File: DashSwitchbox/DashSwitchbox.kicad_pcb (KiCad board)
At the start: 2 copper layers, 16 parts, among them J1 Main Connector, J2 Estop Connector, J3 Dash LVMS, J4 To Drive Mode Button, J5 To Drive Mode Switch, J6 AMS Fault LED, J7 BSPD Fault LED, J8 IMD Fault LED, J9 Inertia Fault LED, U1 LD1117V33

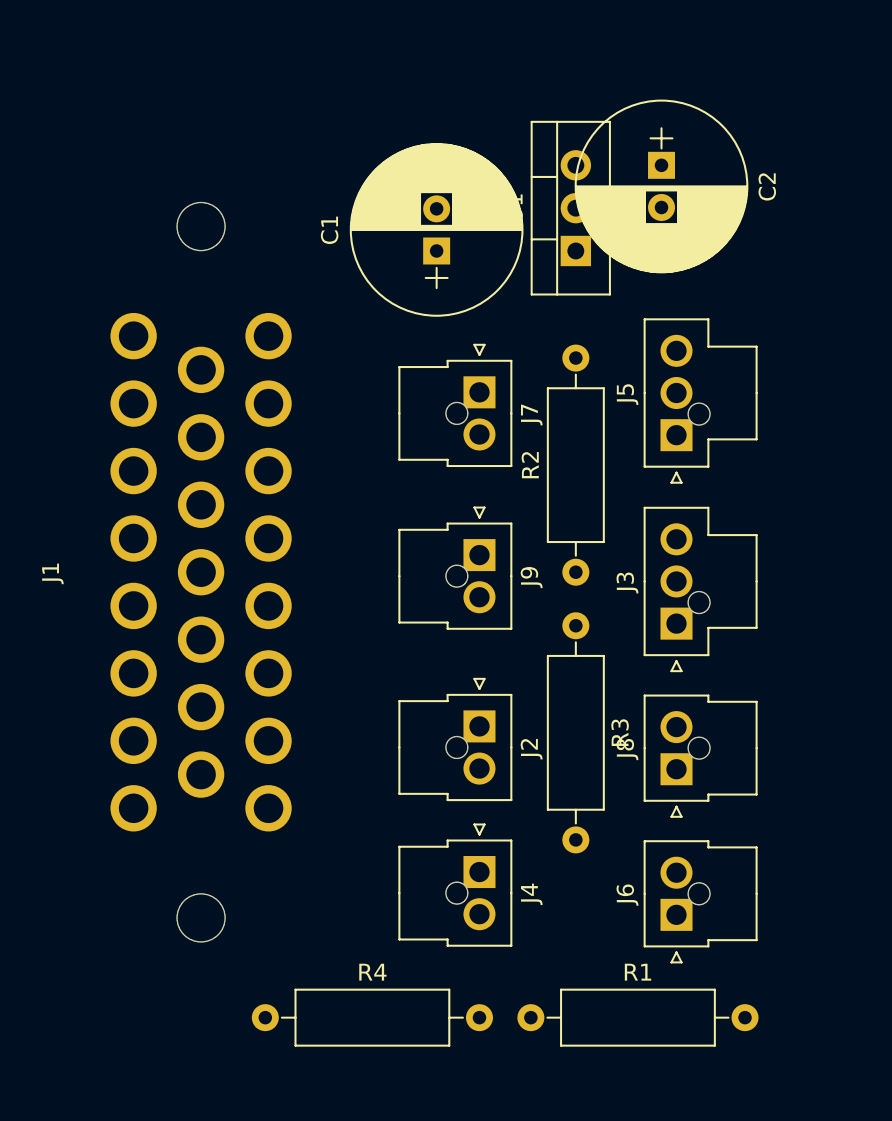
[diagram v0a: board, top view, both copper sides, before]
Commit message: Work for preparation for autorouting
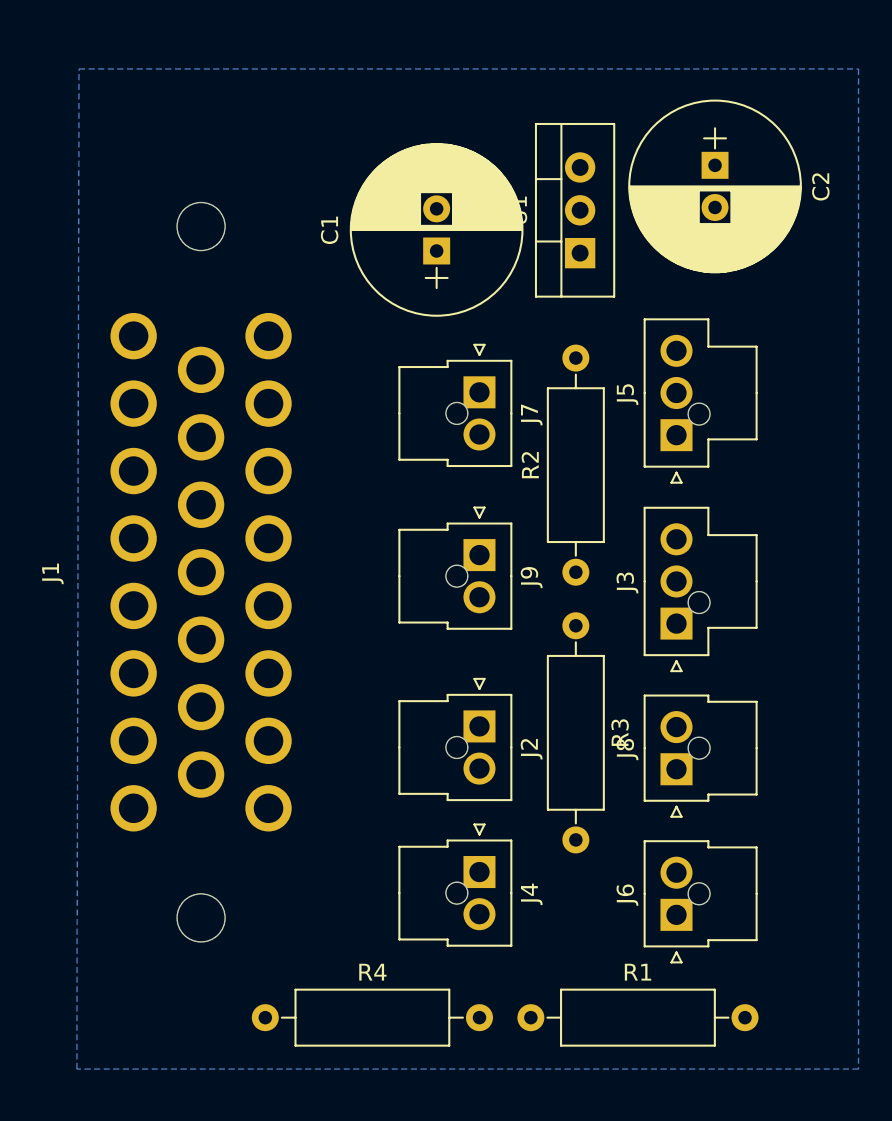
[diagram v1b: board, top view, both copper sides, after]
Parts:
- moved C2 3.17 mm to (123.2, 74.9)
- moved U1 0.28 mm to (115.2, 80.1)
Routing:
- added copper zone on B.Cu, net GND
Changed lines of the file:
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@@
     (links 36)
     (no_connects 36)
-    (area 0 0 0 0)
+    (area 82.845 68.384999 131.699001 129.735001)
     (thickness 1.6)
     (drawings 0)
@@
     (pad_to_mask_clearance 0)
     (aux_axis_origin 0 0)
-    (visible_elements FFFFFF7F)
+    (visible_elements 7FFFFFFF)
     (pcbplotparams
       (layerselection 0x00030_80000001)
@@
   )
   (module TO_SOT_Packages_THT:TO-220-3_Vertical (layer F.Cu)
-    (at 114.935 80.01 90)
+    (at 115.189 80.137 90)
     (descr "TO-220-3, Vertical, RM 2.54mm")
     (tags "TO-220-3 Vertical RM 2.54mm")
@@
   )
   (module Capacitors_THT:CP_Radial_D10.0mm_P2.50mm (layer F.Cu)
-    (at 120.015 74.93 270)
+    (at 123.19 74.93 270)
     (descr "CP, Radial series, Radial, pin pitch=2.50mm, , diameter=10mm, Electrolytic Capacitor")
     (tags "CP Radial series Radial pin pitch 2.50mm  diameter 10mm Electrolytic Capacitor")
@@
     )
   )
+  (zone (net 2) (net_name GND) (layer B.Cu) (hatch edge 0.508)
+    (connect_pads (clearance 0.508))
+    (min_thickness 0.254)
+    (fill (arc_segments 16) (thermal_gap 0.508) (thermal_bridge_width 0.508))
+    (polygon
+      (pts
+        (xy 131.699 128.524) (xy 85.344 128.524) (xy 85.471 69.215) (xy 131.699 69.215)
+      )
+    )
+  )

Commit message: Revise Accumulator HV and LV, route Dash Switchbox, begin PE HV
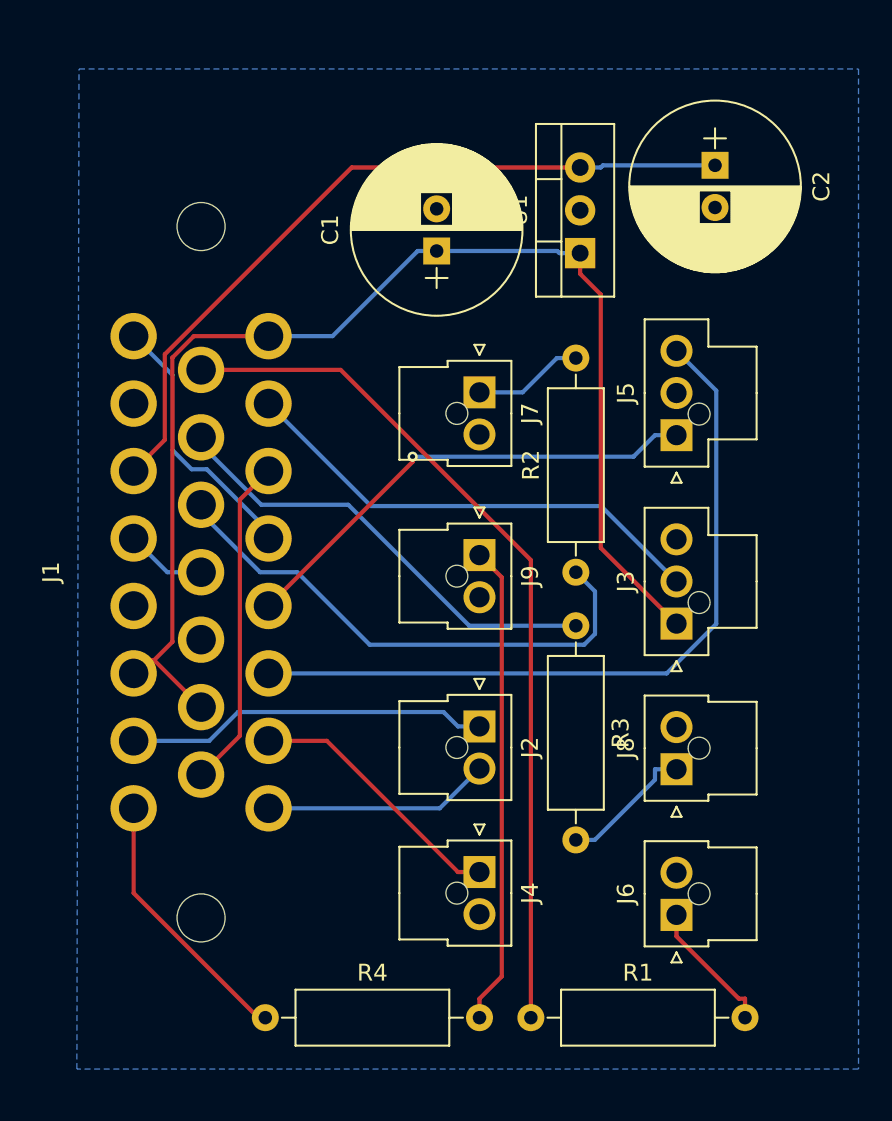
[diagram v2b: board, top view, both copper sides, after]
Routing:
- net +12V: track 0.00 -> 75.1 mm
- net /LED_AMS: track 0.00 -> 51.4 mm
- net +3V3: track 0.00 -> 45.0 mm
- net /BUTTON_2: track 0.00 -> 44.9 mm
- net /LED_BSPD: track 0.00 -> 31.5 mm
- net /BUTTON_1: track 0.00 -> 28.6 mm, vias 0 -> 1
- net /12V_LVMS: track 0.00 -> 28.6 mm
- net Net-(J9-Pad1): track 0.00 -> 28.5 mm
- net /LED_IMD: track 0.00 -> 27.1 mm
- net /AIRS_INERTIA_OUT: track 0.00 -> 21.6 mm
- net /CAN_H: track 0.00 -> 19.7 mm
- net /FLT_INERTIA: track 0.00 -> 15.9 mm
- net /CAN_L: track 0.00 -> 15.8 mm
- net /BUTTON_3: track 0.00 -> 15.7 mm
- net /AIRS_DASH_OUT: track 0.00 -> 13.5 mm
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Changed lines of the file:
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@@
   (general
     (links 36)
-    (no_connects 36)
+    (no_connects 2)
     (area 82.845 68.384999 131.699001 129.735001)
     (thickness 1.6)
     (drawings 0)
-    (tracks 0)
+    (tracks 93)
     (zones 0)
     (modules 16)
@@
     )
   )
+  (segment (start 113.8367 80.01) (end 113.9637 80.137) (width 0.25) (layer B.Cu) (net 1))
+  (segment (start 106.68 80.01) (end 113.8367 80.01) (width 0.25) (layer B.Cu) (net 1))
+  (segment (start 115.189 80.137) (end 113.9637 80.137) (width 0.25) (layer B.Cu) (net 1))
+  (segment (start 100.5047 85.06) (end 105.5547 80.01) (width 0.25) (layer B.Cu) (net 1))
+  (segment (start 96.71 85.06) (end 100.5047 85.06) (width 0.25) (layer B.Cu) (net 1))
+  (segment (start 106.68 80.01) (end 105.5547 80.01) (width 0.25) (layer B.Cu) (net 1))
+  (segment (start 116.4143 82.5876) (end 115.189 81.3623) (width 0.25) (layer F.Cu) (net 1))
+  (segment (start 116.4143 97.6183) (end 116.4143 82.5876) (width 0.25) (layer F.Cu) (net 1))
+  (segment (start 120.904 102.108) (end 116.4143 97.6183) (width 0.25) (layer F.Cu) (net 1))
+  (segment (start 115.189 80.137) (end 115.189 81.3623) (width 0.25) (layer F.Cu) (net 1))
+  (segment (start 92.2791 85.06) (end 96.71 85.06) (width 0.25) (layer F.Cu) (net 1))
+  (segment (start 91.0096 86.3295) (end 92.2791 85.06) (width 0.25) (layer F.Cu) (net 1))
+  (segment (start 91.0096 103.1902) (end 91.0096 86.3295) (width 0.25) (layer F.Cu) (net 1))
+  (segment (start 89.9249 104.2749) (end 91.0096 103.1902) (width 0.25) (layer F.Cu) (net 1))
+  (segment (start 92.71 107.06) (end 89.9249 104.2749) (width 0.25) (layer F.Cu) (net 1))
+  (segment (start 89.4951 104.2749) (end 88.71 105.06) (width 0.25) (layer F.Cu) (net 1))
+  (segment (start 89.9249 104.2749) (end 89.4951 104.2749) (width 0.25) (layer F.Cu) (net 1))
+  (segment (start 116.5413 74.93) (end 116.4143 75.057) (width 0.25) (layer B.Cu) (net 3))
+  (segment (start 123.19 74.93) (end 116.5413 74.93) (width 0.25) (layer B.Cu) (net 3))
+  (segment (start 115.189 75.057) (end 116.4143 75.057) (width 0.25) (layer B.Cu) (net 3))
+  (segment (start 90.5592 91.2108) (end 88.71 93.06) (width 0.25) (layer F.Cu) (net 3))
+  (segment (start 90.5592 86.1367) (end 90.5592 91.2108) (width 0.25) (layer F.Cu) (net 3))
+  (segment (start 101.6389 75.057) (end 90.5592 86.1367) (width 0.25) (layer F.Cu) (net 3))
+  (segment (start 115.189 75.057) (end 101.6389 75.057) (width 0.25) (layer F.Cu) (net 3))
+  (segment (start 107.0926 107.3519) (end 107.9447 108.204) (width 0.25) (layer B.Cu) (net 4))
+  (segment (start 94.9002 107.3519) (end 107.0926 107.3519) (width 0.25) (layer B.Cu) (net 4))
+  (segment (start 93.1921 109.06) (end 94.9002 107.3519) (width 0.25) (layer B.Cu) (net 4))
+  (segment (start 88.71 109.06) (end 93.1921 109.06) (width 0.25) (layer B.Cu) (net 4))
+  (segment (start 109.22 108.204) (end 107.9447 108.204) (width 0.25) (layer B.Cu) (net 4))
+  (segment (start 91.0096 87.3596) (end 88.71 85.06) (width 0.25) (layer B.Cu) (net 5))
+  (segment (start 91.0096 91.8168) (end 91.0096 87.3596) (width 0.25) (layer B.Cu) (net 5))
+  (segment (start 92.1476 92.9548) (end 91.0096 91.8168) (width 0.25) (layer B.Cu) (net 5))
+  (segment (start 93.052 92.9548) (end 92.1476 92.9548) (width 0.25) (layer B.Cu) (net 5))
+  (segment (start 96.71 96.6128) (end 93.052 92.9548) (width 0.25) (layer B.Cu) (net 5))
+  (segment (start 96.71 97.06) (end 96.71 96.6128) (width 0.25) (layer B.Cu) (net 5))
+  (segment (start 90.71 99.06) (end 88.71 97.06) (width 0.25) (layer B.Cu) (net 6))
+  (segment (start 92.71 99.06) (end 90.71 99.06) (width 0.25) (layer B.Cu) (net 6))
+  (segment (start 100.9901 87.06) (end 92.71 87.06) (width 0.25) (layer F.Cu) (net 7))
+  (segment (start 112.268 98.3379) (end 100.9901 87.06) (width 0.25) (layer F.Cu) (net 7))
+  (segment (start 112.268 125.476) (end 112.268 98.3379) (width 0.25) (layer F.Cu) (net 7))
+  (segment (start 116.071 100.196) (end 114.935 99.06) (width 0.25) (layer B.Cu) (net 8))
+  (segment (start 116.071 102.7186) (end 116.071 100.196) (width 0.25) (layer B.Cu) (net 8))
+  (segment (start 115.4276 103.362) (end 116.071 102.7186) (width 0.25) (layer B.Cu) (net 8))
+  (segment (start 102.7124 103.362) (end 115.4276 103.362) (width 0.25) (layer B.Cu) (net 8))
+  (segment (start 98.4104 99.06) (end 102.7124 103.362) (width 0.25) (layer B.Cu) (net 8))
+  (segment (start 96.2099 99.06) (end 98.4104 99.06) (width 0.25) (layer B.Cu) (net 8))
+  (segment (start 92.71 95.5601) (end 96.2099 99.06) (width 0.25) (layer B.Cu) (net 8))
+  (segment (start 92.71 95.06) (end 92.71 95.5601) (width 0.25) (layer B.Cu) (net 8))
+  (segment (start 108.6154 102.235) (end 114.935 102.235) (width 0.25) (layer B.Cu) (net 9))
+  (segment (start 101.4404 95.06) (end 108.6154 102.235) (width 0.25) (layer B.Cu) (net 9))
+  (segment (start 96.2805 95.06) (end 101.4404 95.06) (width 0.25) (layer B.Cu) (net 9))
+  (segment (start 92.71 91.4895) (end 96.2805 95.06) (width 0.25) (layer B.Cu) (net 9))
+  (segment (start 92.71 91.06) (end 92.71 91.4895) (width 0.25) (layer B.Cu) (net 9))
+  (segment (start 95.0096 108.7604) (end 92.71 111.06) (width 0.25) (layer F.Cu) (net 10))
+  (segment (start 95.0096 94.7604) (end 95.0096 108.7604) (width 0.25) (layer F.Cu) (net 10))
+  (segment (start 96.71 93.06) (end 95.0096 94.7604) (width 0.25) (layer F.Cu) (net 10))
+  (segment (start 106.864 113.06) (end 109.22 110.704) (width 0.25) (layer B.Cu) (net 11))
+  (segment (start 96.71 113.06) (end 106.864 113.06) (width 0.25) (layer B.Cu) (net 11))
+  (segment (start 100.1647 109.06) (end 96.71 109.06) (width 0.25) (layer F.Cu) (net 12))
+  (segment (start 107.9447 116.84) (end 100.1647 109.06) (width 0.25) (layer F.Cu) (net 12))
+  (segment (start 109.22 116.84) (end 107.9447 116.84) (width 0.25) (layer F.Cu) (net 12))
+  (via (at 105.253 92.2073) (size 0.6) (layers F.Cu B.Cu) (net 13))
+  (segment (start 120.904 90.932) (end 119.6287 90.932) (width 0.25) (layer B.Cu) (net 13))
+  (segment (start 118.3534 92.2073) (end 119.6287 90.932) (width 0.25) (layer B.Cu) (net 13))
+  (segment (start 105.253 92.2073) (end 118.3534 92.2073) (width 0.25) (layer B.Cu) (net 13))
+  (segment (start 105.2529 92.2073) (end 105.253 92.2073) (width 0.25) (layer F.Cu) (net 13))
+  (segment (start 105.2529 92.5171) (end 105.2529 92.2073) (width 0.25) (layer F.Cu) (net 13))
+  (segment (start 96.71 101.06) (end 105.2529 92.5171) (width 0.25) (layer F.Cu) (net 13))
+  (segment (start 123.2625 88.2905) (end 120.904 85.932) (width 0.25) (layer B.Cu) (net 14))
+  (segment (start 123.2625 102.1186) (end 123.2625 88.2905) (width 0.25) (layer B.Cu) (net 14))
+  (segment (start 120.3211 105.06) (end 123.2625 102.1186) (width 0.25) (layer B.Cu) (net 14))
+  (segment (start 96.71 105.06) (end 120.3211 105.06) (width 0.25) (layer B.Cu) (net 14))
+  (segment (start 116.4328 95.1368) (end 120.904 99.608) (width 0.25) (layer B.Cu) (net 15))
+  (segment (start 102.7868 95.1368) (end 116.4328 95.1368) (width 0.25) (layer B.Cu) (net 15))
+  (segment (start 96.71 89.06) (end 102.7868 95.1368) (width 0.25) (layer B.Cu) (net 15))
+  (segment (start 124.5994 124.3507) (end 124.968 124.3507) (width 0.25) (layer F.Cu) (net 16))
+  (segment (start 120.904 120.6553) (end 124.5994 124.3507) (width 0.25) (layer F.Cu) (net 16))
+  (segment (start 120.904 119.38) (end 120.904 120.6553) (width 0.25) (layer F.Cu) (net 16))
+  (segment (start 124.968 125.476) (end 124.968 124.3507) (width 0.25) (layer F.Cu) (net 16))
+  (segment (start 111.7777 88.392) (end 113.8097 86.36) (width 0.25) (layer B.Cu) (net 17))
+  (segment (start 109.22 88.392) (end 111.7777 88.392) (width 0.25) (layer B.Cu) (net 17))
+  (segment (start 114.935 86.36) (end 113.8097 86.36) (width 0.25) (layer B.Cu) (net 17))
+  (segment (start 119.6287 111.3666) (end 116.0603 114.935) (width 0.25) (layer B.Cu) (net 18))
+  (segment (start 119.6287 110.744) (end 119.6287 111.3666) (width 0.25) (layer B.Cu) (net 18))
+  (segment (start 114.935 114.935) (end 116.0603 114.935) (width 0.25) (layer B.Cu) (net 18))
+  (segment (start 120.904 110.744) (end 119.6287 110.744) (width 0.25) (layer B.Cu) (net 18))
+  (segment (start 110.5418 123.0289) (end 109.22 124.3507) (width 0.25) (layer F.Cu) (net 19))
+  (segment (start 110.5418 99.3658) (end 110.5418 123.0289) (width 0.25) (layer F.Cu) (net 19))
+  (segment (start 109.22 98.044) (end 110.5418 99.3658) (width 0.25) (layer F.Cu) (net 19))
+  (segment (start 109.22 125.476) (end 109.22 124.3507) (width 0.25) (layer F.Cu) (net 19))
+  (segment (start 96.1008 125.476) (end 96.52 125.476) (width 0.25) (layer F.Cu) (net 20))
+  (segment (start 88.71 118.0852) (end 96.1008 125.476) (width 0.25) (layer F.Cu) (net 20))
+  (segment (start 88.71 113.06) (end 88.71 118.0852) (width 0.25) (layer F.Cu) (net 20))
   (zone (net 2) (net_name GND) (layer B.Cu) (hatch edge 0.508)
     (connect_pads (clearance 0.508))
     (min_thickness 0.254)
-    (fill (arc_segments 16) (thermal_gap 0.508) (thermal_bridge_width 0.508))
+    (fill yes (arc_segments 16) (thermal_gap 0.508) (thermal_bridge_width 0.508))
     (polygon
       (pts

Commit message: Tweak routing on boards, add mounting holes to dash switchbox
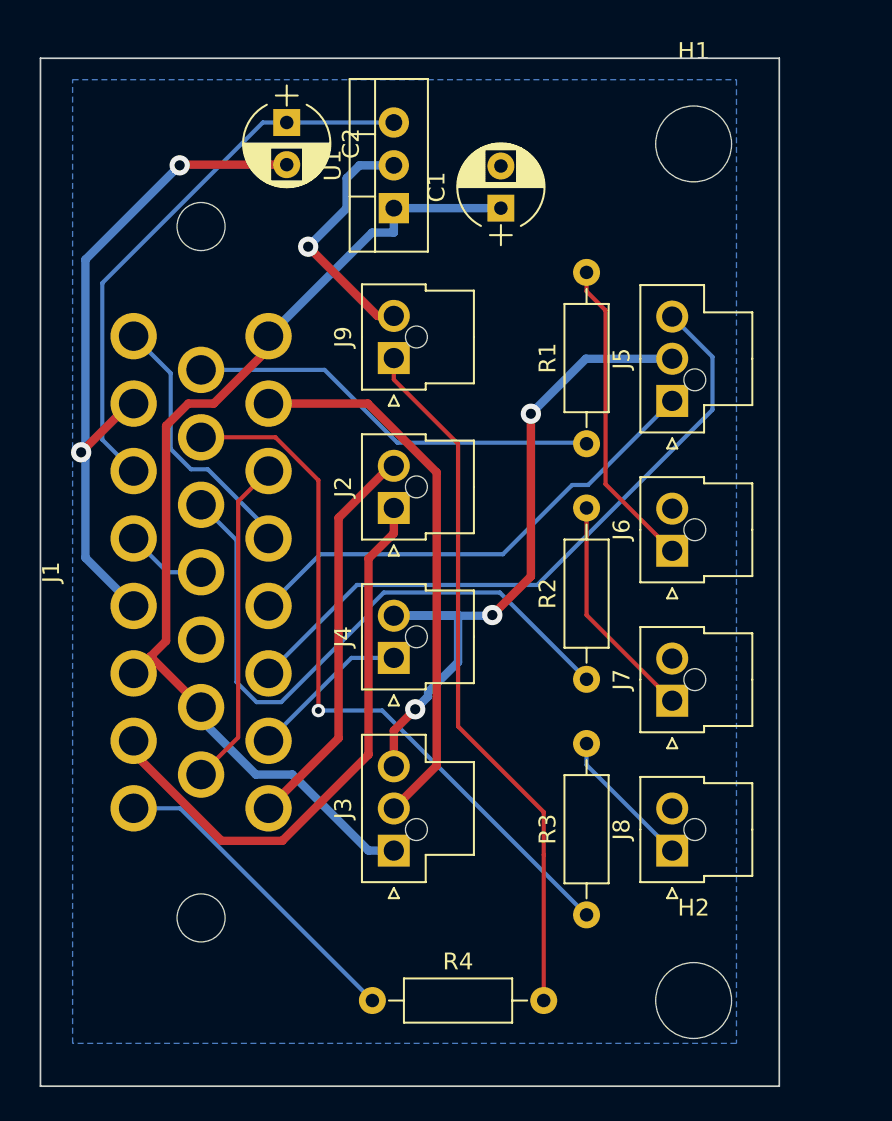
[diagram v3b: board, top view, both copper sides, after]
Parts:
- added H1: MtngHole, Mounting_Holes:MountingHole_4.5mm, F.Cu at (121.9, 73.7)
- added H2: MtngHole, Mounting_Holes:MountingHole_4.5mm, F.Cu at (121.9, 124.5)
- C1, C2: footprint Capacitors_THT:CP_Radial_D10.0mm_P2.50mm -> Capacitors_THT:CP_Radial_D5.0mm_P2.50mm
- R1, R2, R3, R4: footprint Resistors_THT:R_Axial_DIN0309_L9.0mm_D3.2mm_P12.70mm_Horizontal -> Resistors_THT:R_Axial_DIN0207_L6.3mm_D2.5mm_P10.16mm_Horizontal
- moved R1 34.2 mm to (115.6, 91.4), turned to 90 degrees
- moved C2 25.5 mm to (97.8, 72.4)
- moved J6 21.6 mm to (120.7, 97.8)
- moved J7 21.6 mm to (120.7, 106.7), turned to 90 degrees
- moved J3 21.5 mm to (104.1, 115.6)
- moved R3 17.2 mm to (115.6, 119.4), turned to 90 degrees
- moved J2 13.9 mm to (104.1, 95.2), turned to 90 degrees
- moved J4 13.7 mm to (104.1, 104.1), turned to 90 degrees
- moved J9 12.7 mm to (104.1, 86.4), turned to 90 degrees
- moved U1 11.4 mm to (104.1, 77.5)
- moved R4 6.43 mm to (102.9, 124.5)
- moved R2 6.38 mm to (115.6, 105.4)
- moved J8 4.83 mm to (120.7, 115.6)
- moved C1 4.58 mm to (110.5, 77.5)
- moved J5 2.05 mm to (120.7, 88.9)
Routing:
- net GND: track 0.00 -> 98.3 mm, vias 0 -> 6
- net /LED_AMS: track 51.4 -> 24.7 mm
- net /LED_IMD: track 27.1 -> 42.6 mm, vias 0 -> 1
- net +12V: track 75.1 -> 61.6 mm
- net Net-(J9-Pad1): track 28.5 -> 41.8 mm
- net /AIRS_INERTIA_OUT: track 21.6 -> 34.2 mm
- net +3V3: track 45.0 -> 33.1 mm
- net Net-(J6-Pad1): track 8.00 -> 18.6 mm
- net /AIRS_DASH_OUT: track 13.5 -> 23.5 mm
- net Net-(J7-Pad1): track 6.56 -> 13.5 mm
- net /BUTTON_3: track 15.7 -> 9.47 mm
- net /LED_BSPD: track 31.5 -> 37.7 mm
- net /BUTTON_2: track 44.9 -> 39.3 mm
- net /12V_LVMS: track 28.6 -> 32.6 mm
- net /FLT_INERTIA: track 15.9 -> 18.9 mm
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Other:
- board outline added: 43.8 x 61 mm
- net class Default: via_dia 0.6 -> 0.8
- net class Power added: clearance 0.3, trace_width 0.5, via_dia 1.2, via_drill 0.6
